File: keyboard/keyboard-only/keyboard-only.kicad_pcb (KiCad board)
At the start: 2 copper layers, 3.6 x 3.1 mm, 203 parts, among them J1 USB_C_Receptacle_USB2.0, SW1 SW_PUSH, SW10 SW_PUSH, SW11 SW_PUSH, SW12 SW_PUSH, SW13 SW_PUSH, SW14 SW_PUSH, SW15 SW_PUSH, SW16 SW_PUSH, SW17 SW_PUSH, SW18 SW_PUSH, SW19 SW_PUSH, SW2 SW_PUSH, SW20 SW_PUSH, SW21 SW_PUSH, SW22 SW_PUSH, SW23 SW_PUSH, SW24 SW_PUSH, SW25 SW_PUSH, SW26 SW_PUSH, SW27 SW_PUSH, SW28 SW_PUSH, SW29 SW_PUSH, SW3 SW_PUSH, SW30 SW_PUSH, SW31 SW_PUSH, SW32 SW_PUSH, SW33 SW_PUSH, SW34 SW_PUSH, SW35 SW_PUSH, SW36 SW_PUSH, SW37 SW_PUSH, SW38 SW_PUSH, SW39 SW_PUSH, SW4 SW_PUSH, SW40 SW_PUSH, SW41 SW_PUSH, SW42 SW_PUSH, SW43 SW_PUSH, SW44 SW_PUSH, SW45 SW_PUSH, SW46 SW_PUSH, SW47 SW_PUSH, SW48 SW_PUSH, SW49 SW_PUSH, SW5 SW_PUSH, SW50 SW_PUSH, SW51 SW_PUSH, SW52 SW_PUSH, SW53 SW_PUSH, SW54 SW_PUSH, SW55 SW_PUSH, SW56 SW_PUSH, SW57 SW_PUSH, SW58 SW_PUSH, SW59 SW_PUSH, SW6 SW_PUSH, SW60 SW_PUSH, SW7 SW_PUSH, SW8 SW_PUSH, SW9 SW_PUSH, U1 ATmega16U4-AU, Y1 16MHz

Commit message: Add net name for rows and columns
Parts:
- moved LED53 260.5 mm to (29.4, 144.7)
- moved D62 249.8 mm to (19.3, 158.1)
- moved LED49 242.1 mm to (20.5, 149.5)
- moved LED4 236.5 mm to (56.2, 149.5)
- moved SW8 233.9 mm to (26.1, 112.0)
- moved LED47 225.6 mm to (38.3, 144.7)
- moved D34 224.7 mm to (45.5, 158.1)
- moved D35 216.4 mm to (236.8, 75.6)
- moved LED57 200.8 mm to (91.8, 149.5)
- moved D59 189.7 mm to (71.7, 158.1)
- moved LED30 189.6 mm to (222.5, 73.5)
- moved SW38 188.8 mm to (86.7, 91.8)
- moved D10 179.4 mm to (221.3, 87.4)
- moved D48 177.2 mm to (78.2, 158.1)
- moved SW28 175.6 mm to (207.9, 31.2)
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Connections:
- D10 pad 1: N$35 -> ROW0
- D10 pad 2: N$17 -> N$27
- D11 pad 1: N$38 (its old number) -> ROW0
- D11 pad 2: N$17 -> N$29
- D12 pad 1: N$41 -> ROW0
- D12 pad 2: N$17 -> N$31
- D13 pad 1: N$44 (its old number) -> ROW0
- D13 pad 2: N$17 -> N$33
- D14 pad 1: N$47 -> ROW0
- D14 pad 2: N$17 -> N$35
- D15 pad 1: N$50 (its old number) -> ROW0
- D15 pad 2: N$17 -> N$37
- D16 pad 1: N$52 (its old number) -> ROW1
- D16 pad 2: N$53 -> N$39
- D17 pad 1: N$55 -> ROW1
- D17 pad 2: N$53 -> N$41
- D18 pad 1: N$57 -> ROW1
- D18 pad 2: N$53 -> N$43
- D19 pad 1: N$59 -> ROW1
- D19 pad 2: N$53 -> N$45
- D20 pad 1: N$61 -> ROW1
- D20 pad 2: N$53 -> N$47
- D21 pad 1: N$63 -> ROW1
- D21 pad 2: N$53 -> N$49
- D22 pad 1: N$65 -> ROW1
- D22 pad 2: N$53 -> N$51
- D23 pad 1: N$67 -> ROW1
- D24 pad 1: N$69 -> ROW1
- D24 pad 2: N$53 -> N$55
- D25 pad 1: N$71 -> ROW1
- D25 pad 2: N$53 -> N$57
- D26 pad 1: N$73 -> ROW1
- D26 pad 2: N$53 -> N$59
- D27 pad 1: N$75 -> ROW1
- D27 pad 2: N$53 -> N$61
- D28 pad 1: N$77 -> ROW2
- D28 pad 2: N$78 (its old number) -> N$63
- D29 pad 1: N$80 (its old number) -> ROW2
- D29 pad 2: N$78 (its old number) -> N$65
- D30 pad 1: N$82 (its old number) -> ROW2
- D30 pad 2: N$78 (its old number) -> N$67
- D31 pad 1: N$84 (its old number) -> ROW2
- D31 pad 2: N$78 (its old number) -> N$69
- D32 pad 1: N$86 (its old number) -> ROW2
- D32 pad 2: N$78 (its old number) -> N$71
- D33 pad 1: N$88 (its old number) -> ROW2
- D33 pad 2: N$78 (its old number) -> N$73
- D34 pad 1: N$90 (its old number) -> ROW2
- D34 pad 2: N$78 (its old number) -> N$75
- D35 pad 1: N$92 (its old number) -> ROW2
- D35 pad 2: N$78 (its old number) -> N$77
- D36 pad 1: N$94 (its old number) -> ROW2
- D36 pad 2: N$78 (its old number) -> N$79
- D37 pad 1: N$96 (its old number) -> ROW2
- D37 pad 2: N$78 (its old number) -> N$81
- D38 pad 1: N$98 (its old number) -> ROW2
- D38 pad 2: N$78 (its old number) -> N$83
- D39 pad 1: N$100 (its old number) -> ROW2
- D39 pad 2: N$78 (its old number) -> N$85
- D4 pad 1: N$16 (its old number) -> ROW0
- D4 pad 2: N$17 -> N$15
- D40 pad 1: N$102 (its old number) -> ROW3
- D40 pad 2: N$103 -> N$87
- D41 pad 1: N$105 -> ROW3
- D41 pad 2: N$103 -> N$89
- D42 pad 1: N$107 -> ROW3
- D42 pad 2: N$103 -> N$91
- D43 pad 1: N$109 -> ROW3
- D43 pad 2: N$103 -> N$93
- D44 pad 1: N$111 -> ROW3
- D44 pad 2: N$103 -> N$95
- D45 pad 1: N$113 -> ROW3
- D45 pad 2: N$103 -> N$97
- D46 pad 1: N$115 -> ROW3
- D46 pad 2: N$103 -> N$99
- D47 pad 1: N$117 -> ROW3
- D47 pad 2: N$103 -> N$101
- D48 pad 1: N$119 -> ROW3
- D49 pad 1: N$121 -> ROW3
- D49 pad 2: N$103 -> N$105
- D5 pad 1: N$20 (its old number) -> ROW0
- D50 pad 1: N$123 -> ROW3
- D50 pad 2: N$103 -> N$107
- D51 pad 1: N$125 -> ROW3
- D51 pad 2: N$103 -> N$109
- D52 pad 1: N$127 -> ROW4
- D52 pad 2: N$128 (its old number) -> N$111
- D53 pad 1: N$130 (its old number) -> ROW4
- D53 pad 2: N$128 (its old number) -> N$113
- D54 pad 1: N$132 (its old number) -> ROW4
- D54 pad 2: N$128 (its old number) -> N$115
- D55 pad 1: N$134 (its old number) -> ROW4
- D55 pad 2: N$128 (its old number) -> N$117
- D56 pad 1: N$136 -> ROW4
- D56 pad 2: N$128 (its old number) -> N$119
- D57 pad 1: N$138 -> ROW4
- D57 pad 2: N$128 (its old number) -> N$121
- D58 pad 1: N$140 -> ROW4
- D58 pad 2: N$128 (its old number) -> N$123
- D59 pad 1: N$142 -> ROW4
- D59 pad 2: N$128 (its old number) -> N$125
- D6 pad 1: N$23 -> ROW0
- D6 pad 2: N$17 -> N$19
- D60 pad 1: N$144 -> ROW4
- D60 pad 2: N$128 (its old number) -> N$127
- D61 pad 1: N$146 -> ROW4
- D61 pad 2: N$128 (its old number) -> N$129
- D62 pad 1: N$148 -> ROW4
- D62 pad 2: N$128 (its old number) -> N$131
- D63 pad 1: N$150 -> ROW4
- D63 pad 2: N$128 (its old number) -> N$133
- D7 pad 1: N$26 (its old number) -> ROW0
- D7 pad 2: N$17 -> N$21
- D8 pad 1: N$29 -> ROW0
- D8 pad 2: N$17 -> N$23
- D9 pad 1: N$32 (its old number) -> ROW0
- D9 pad 2: N$17 -> N$25
- SW1 pad 1: N$15 -> COL0
- SW1 pad 2: N$16 (its old number) -> N$15
- SW10 pad 1: N$43 -> COL9
- SW10 pad 2: N$44 (its old number) -> N$33
- SW11 pad 1: N$46 (its old number) -> COL10
- SW11 pad 2: N$47 -> N$35
- SW12 pad 1: N$49 -> COL11
- SW12 pad 2: N$50 (its old number) -> N$37
- SW13 pad 1: N$15 -> COL0
- SW13 pad 2: N$52 (its old number) -> N$39
- SW14 pad 1: N$19 -> COL1
- SW14 pad 2: N$55 -> N$41
- SW15 pad 1: N$22 (its old number) -> COL2
- SW15 pad 2: N$57 -> N$43
- SW16 pad 1: N$25 -> COL3
- SW16 pad 2: N$59 -> N$45
- SW17 pad 1: N$28 (its old number) -> COL4
- SW17 pad 2: N$61 -> N$47
- SW18 pad 1: N$31 -> COL5
- SW18 pad 2: N$63 -> N$49
- SW19 pad 1: N$34 (its old number) -> COL6
- SW19 pad 2: N$65 -> N$51
- SW2 pad 1: N$19 -> COL1
- SW2 pad 2: N$20 (its old number) -> N$17
- SW20 pad 1: N$37 -> COL7
- SW20 pad 2: N$67 -> N$53
- SW21 pad 1: N$40 (its old number) -> COL8
- SW21 pad 2: N$69 -> N$55
- SW22 pad 1: N$43 -> COL9
- SW22 pad 2: N$71 -> N$57
- SW23 pad 1: N$46 (its old number) -> COL10
- SW23 pad 2: N$73 -> N$59
- SW24 pad 1: N$49 -> COL11
- SW24 pad 2: N$75 -> N$61
- SW25 pad 1: N$15 -> COL0
- SW25 pad 2: N$77 -> N$63
- SW26 pad 1: N$19 -> COL1
- SW26 pad 2: N$80 (its old number) -> N$65
- SW27 pad 1: N$22 (its old number) -> COL2
- SW27 pad 2: N$82 (its old number) -> N$67
- SW28 pad 1: N$25 -> COL3
- SW28 pad 2: N$84 (its old number) -> N$69
- SW29 pad 1: N$28 (its old number) -> COL4
- SW29 pad 2: N$86 (its old number) -> N$71
- SW3 pad 1: N$22 (its old number) -> COL2
- SW3 pad 2: N$23 -> N$19
- SW30 pad 1: N$31 -> COL5
- SW30 pad 2: N$88 (its old number) -> N$73
- SW31 pad 1: N$34 (its old number) -> COL6
- SW31 pad 2: N$90 (its old number) -> N$75
- SW32 pad 1: N$37 -> COL7
- SW32 pad 2: N$92 (its old number) -> N$77
- SW33 pad 1: N$40 (its old number) -> COL8
- SW33 pad 2: N$94 (its old number) -> N$79
- SW34 pad 1: N$43 -> COL9
- SW34 pad 2: N$96 (its old number) -> N$81
- SW35 pad 1: N$46 (its old number) -> COL10
- SW35 pad 2: N$98 (its old number) -> N$83
- SW36 pad 1: N$49 -> COL11
- SW36 pad 2: N$100 (its old number) -> N$85
- SW37 pad 1: N$15 -> COL0
- SW37 pad 2: N$102 (its old number) -> N$87
- SW38 pad 1: N$19 -> COL1
- SW38 pad 2: N$105 -> N$89
- SW39 pad 1: N$22 (its old number) -> COL2
- SW39 pad 2: N$107 -> N$91
- SW4 pad 1: N$25 -> COL3
- SW4 pad 2: N$26 (its old number) -> N$21
- SW40 pad 1: N$25 -> COL3
- SW40 pad 2: N$109 -> N$93
- SW41 pad 1: N$28 (its old number) -> COL4
- SW41 pad 2: N$111 -> N$95
- SW42 pad 1: N$31 -> COL5
- SW42 pad 2: N$113 -> N$97
- SW43 pad 1: N$34 (its old number) -> COL6
- SW43 pad 2: N$115 -> N$99
- SW44 pad 1: N$37 -> COL7
- SW44 pad 2: N$117 -> N$101
- SW45 pad 1: N$40 (its old number) -> COL8
- SW45 pad 2: N$119 -> N$103
- SW46 pad 1: N$43 -> COL9
- SW46 pad 2: N$121 -> N$105
- SW47 pad 1: N$46 (its old number) -> COL10
- SW47 pad 2: N$123 -> N$107
- SW48 pad 1: N$49 -> COL11
- SW48 pad 2: N$125 -> N$109
- SW49 pad 1: N$15 -> COL0
- SW49 pad 2: N$127 -> N$111
- SW5 pad 1: N$28 (its old number) -> COL4
- SW5 pad 2: N$29 -> N$23
- SW50 pad 1: N$19 -> COL1
- SW50 pad 2: N$130 (its old number) -> N$113
- SW51 pad 1: N$22 (its old number) -> COL2
- SW51 pad 2: N$132 (its old number) -> N$115
- SW52 pad 1: N$25 -> COL3
- SW52 pad 2: N$134 (its old number) -> N$117
- SW53 pad 1: N$28 (its old number) -> COL4
- SW53 pad 2: N$136 -> N$119
- SW54 pad 1: N$31 -> COL5
- SW54 pad 2: N$138 -> N$121
- SW55 pad 1: N$34 (its old number) -> COL6
- SW55 pad 2: N$140 -> N$123
- SW56 pad 1: N$37 -> COL7
- SW56 pad 2: N$142 -> N$125
- SW57 pad 1: N$40 (its old number) -> COL8
- SW57 pad 2: N$144 -> N$127
- SW58 pad 1: N$43 -> COL9
- SW58 pad 2: N$146 -> N$129
- SW59 pad 1: N$46 (its old number) -> COL10
- SW59 pad 2: N$148 -> N$131
- SW6 pad 1: N$31 -> COL5
- SW6 pad 2: N$32 (its old number) -> N$25
- SW60 pad 1: N$49 -> COL11
- SW60 pad 2: N$150 -> N$133
- SW7 pad 1: N$34 (its old number) -> COL6
- SW7 pad 2: N$35 -> N$27
- SW8 pad 1: N$37 -> COL7
- SW8 pad 2: N$38 (its old number) -> N$29
- SW9 pad 1: N$40 (its old number) -> COL8
- SW9 pad 2: N$41 -> N$31
- U1 pad 1: N$103 -> ROW3
- U1 pad 10: N$37 -> COL7
- U1 pad 11: N$40 (its old number) -> COL8
- U1 pad 12: N$49 -> COL11
- U1 pad 25: N$17 -> ROW0
- U1 pad 27: N$78 (its old number) -> ROW2
- U1 pad 28: N$128 (its old number) -> ROW4
- U1 pad 29: N$43 -> COL9
- U1 pad 30: N$46 (its old number) -> COL10
- U1 pad 31: N$53 -> ROW1
- U1 pad 36: N$31 -> COL5
- U1 pad 37: N$28 (its old number) -> COL4
- U1 pad 38: N$25 -> COL3
- U1 pad 39: N$22 (its old number) -> COL2
- U1 pad 40: N$19 -> COL1
- U1 pad 41: N$15 -> COL0
- U1 pad 9: N$34 (its old number) -> COL6

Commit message: Flip everything to bottom of pcb
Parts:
- C1, C2, C3, C4, C5, C6, C7, C8, D1, D10, D11, D12, D13, D14, D15, D16, D17, D18, D19, D2, D20, D21, D22, D23, D24, D25, D26, D27, D28, D29, D3, D30, D31, D32, D33, D34, D35, D36, D37, D38, D39, D4, D40, D41, D42, D43, D44, D45, D46, D47, D48, D49, D5, D50, D51, D52, D53, D54, D55, D56, D57, D58, D59, D6, D60, D61, D62, D63, D7, D8, D9, F1, J1, LED1, LED10, LED11, LED12, LED13, LED14, LED15, LED16, LED17, LED18, LED19, LED2, LED20, LED21, LED22, LED23, LED24, LED25, LED26, LED27, LED28, LED29, LED3, LED30, LED31, LED32, LED33, LED34, LED35, LED36, LED37, LED38, LED39, LED4, LED40, LED41, LED42, LED43, LED44, LED45, LED46, LED47, LED48, LED49, LED5, LED50, LED51, LED52, LED53, LED54, LED55, LED56, LED57, LED58, LED59, LED6, LED60, LED7, LED8, LED9, R1, R2, R3, R4, R5, R6, R7, R8, U1, Y1: moved to B.Cu

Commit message: Organize key matrix and diodes
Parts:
- moved D62 240.1 mm to (254.0, 107.3), turned to 90 degrees
- moved R2 238.6 mm to (40.6, 40.0)
- moved R1 238.5 mm to (40.7, 35.3)
- moved J1 232.6 mm to (38.1, 26.0)
- moved SW12 223.1 mm to (265.4, 31.1)
- moved SW36 222.4 mm to (265.4, 69.2)
- moved SW11 220.3 mm to (246.4, 31.1)
- moved SW35 209.7 mm to (246.4, 69.2)
- moved D50 207.5 mm to (254.0, 88.3), turned to 90 degrees
- moved D52 194.1 mm to (63.5, 107.3), turned to 90 degrees
- moved LED10 188.2 mm to (202.1, 225.3)
- moved LED30 188.2 mm to (172.9, 255.2)
- moved LED31 188.2 mm to (193.1, 239.8)
- moved LED35 188.2 mm to (193.1, 225.3)
- moved LED44 188.2 mm to (181.9, 250.3)
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
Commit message: Setup LEDs
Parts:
- moved LED49 334.0 mm to (227.3, 55.2)
- moved LED53 329.7 mm to (246.4, 74.3)
- moved LED48 326.1 mm to (227.3, 74.3)
- moved LED60 312.8 mm to (265.4, 36.2)
- moved LED54 304.7 mm to (246.4, 93.3)
- moved LED47 295.9 mm to (227.3, 93.3)
- moved LED59 293.5 mm to (265.4, 55.3)
- moved LED52 289.5 mm to (246.4, 55.2)
- moved LED38 289.1 mm to (189.2, 74.3)
- moved LED46 289.1 mm to (227.3, 112.4)
- moved LED57 285.2 mm to (265.4, 93.3)
- moved LED58 284.5 mm to (265.4, 74.3)
- moved LED56 277.9 mm to (265.4, 112.4)
- moved LED39 267.6 mm to (189.2, 55.2)
- moved LED50 266.7 mm to (227.3, 36.2)
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
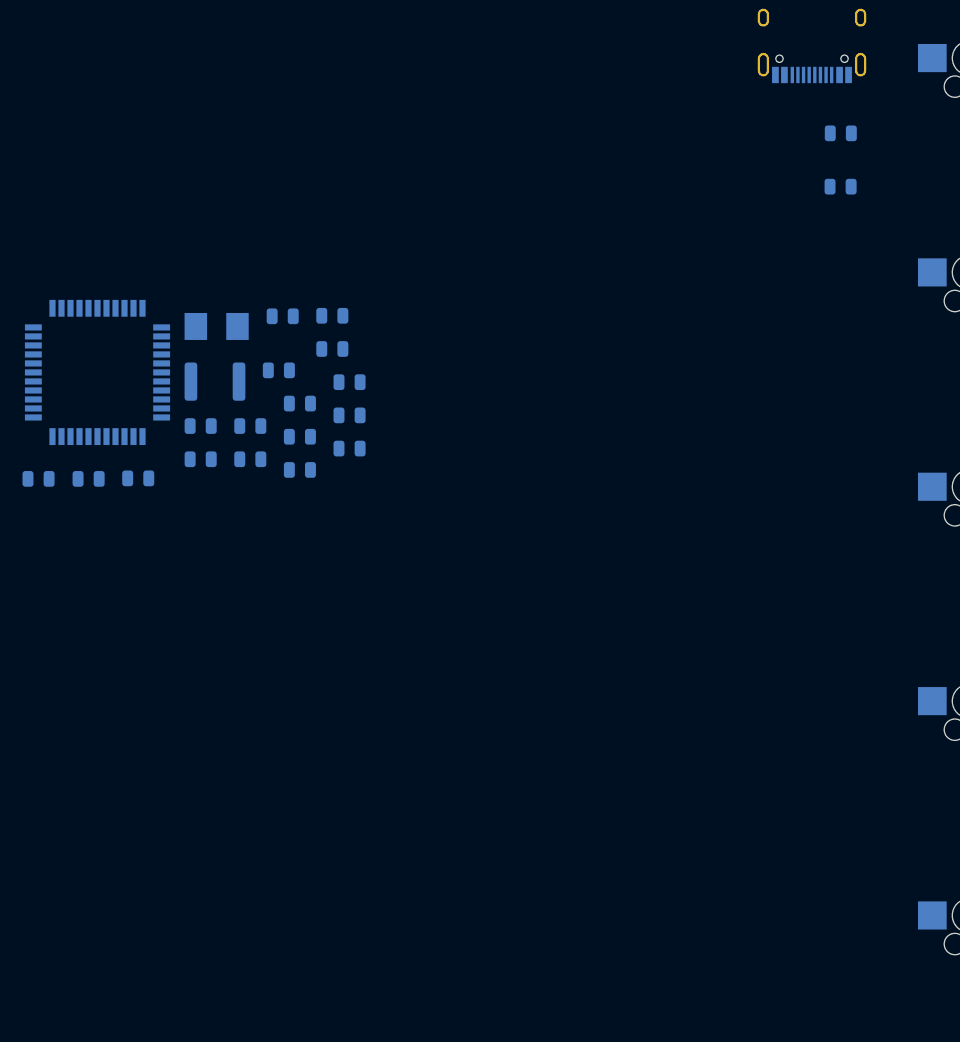
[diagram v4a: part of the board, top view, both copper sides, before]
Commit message: Base ProMicro layout
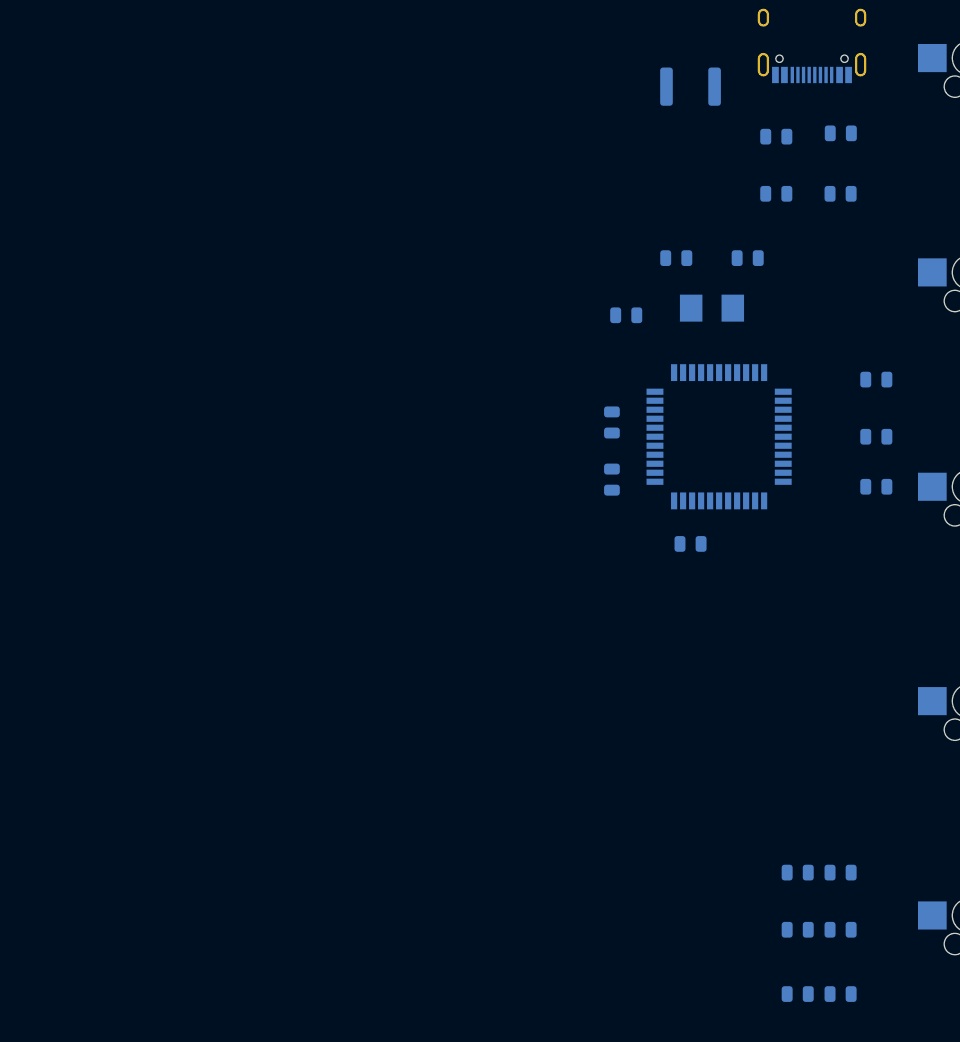
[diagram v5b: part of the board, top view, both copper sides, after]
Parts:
- moved D1 81.0 mm to (40.6, 111.8)
- moved D3 79.4 mm to (40.6, 101.0)
- moved D2 73.7 mm to (40.6, 106.0)
- moved R5 68.3 mm to (36.8, 101.0)
- moved R4 67.6 mm to (36.8, 106.0)
- moved R3 62.7 mm to (36.8, 111.8)
- moved C2 55.7 mm to (43.8, 62.2)
- moved U1 55.5 mm to (29.8, 62.2)
- moved R8 53.4 mm to (34.9, 35.6)
- moved C4 51.4 mm to (43.8, 66.7)
- moved F1 49.7 mm to (27.3, 31.1), turned to 180 degrees
- moved C3 48.7 mm to (43.8, 57.1)
- moved Y1 44.1 mm to (29.2, 50.8), turned to 180 degrees
- moved C7 42.8 mm to (32.4, 46.4)
- moved R7 42.7 mm to (34.9, 40.6)
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
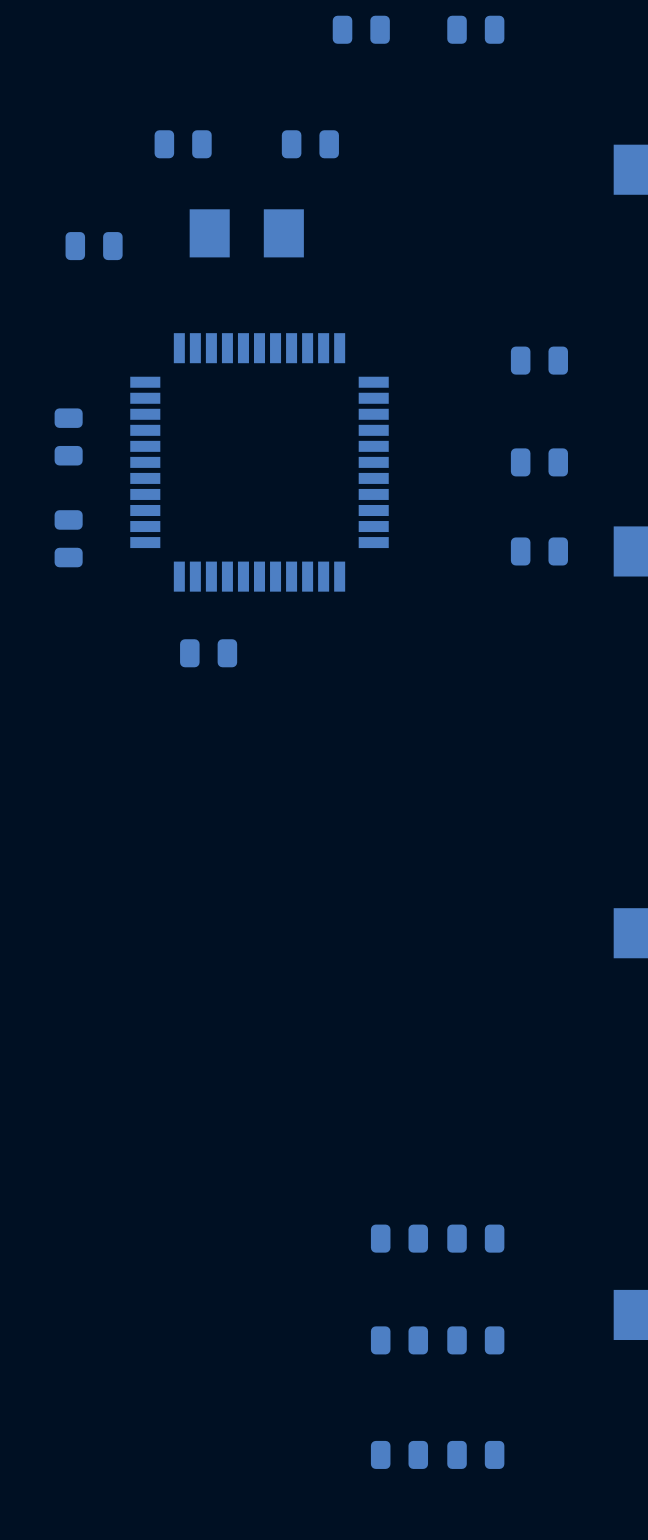
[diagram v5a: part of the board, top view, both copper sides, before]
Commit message: Reorient LEDs
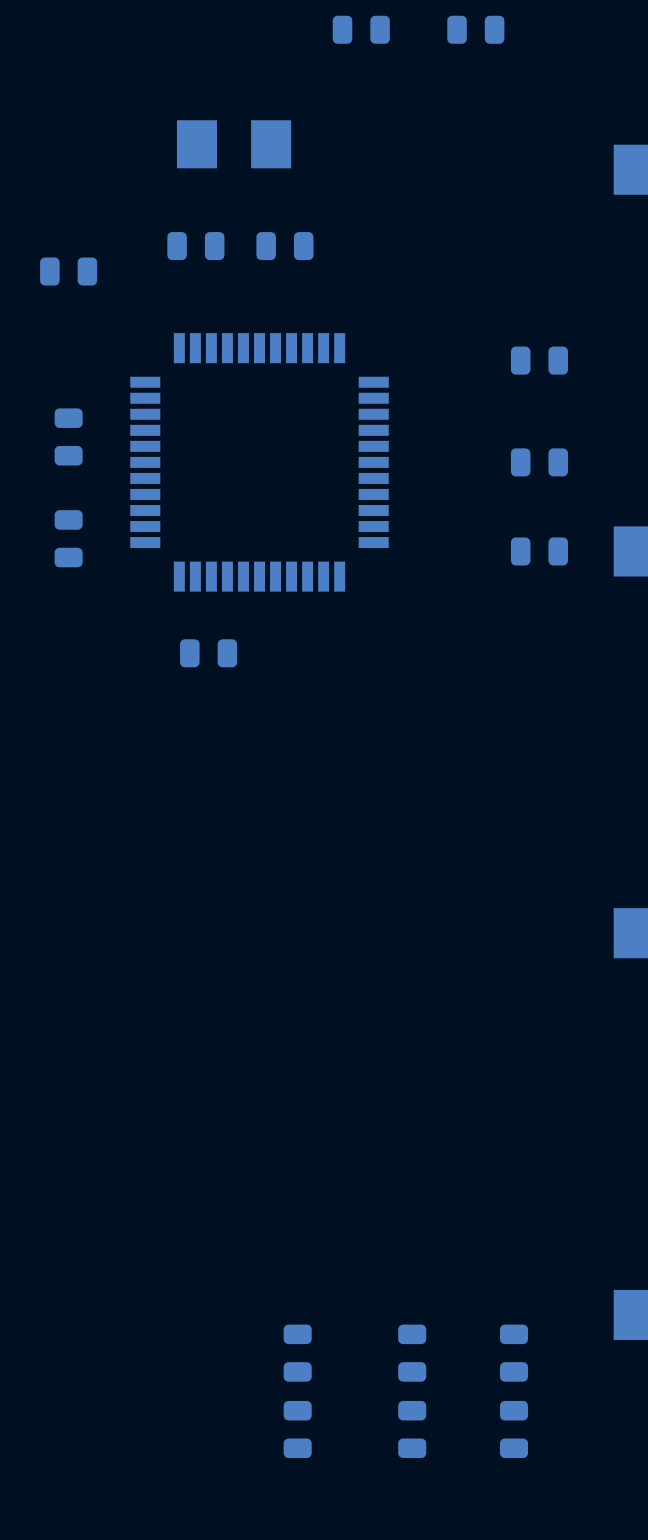
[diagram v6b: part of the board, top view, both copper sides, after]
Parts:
- moved D3 9.71 mm to (42.5, 110.5), turned to 270 degrees
- moved D1 8.98 mm to (31.8, 110.5), turned to 270 degrees
- moved R5 8.08 mm to (42.5, 106.7), turned to 270 degrees
- moved R3 7.18 mm to (31.8, 106.7), turned to 270 degrees
- moved D2 5.46 mm to (37.5, 110.5), turned to 270 degrees
- moved C7 5.24 mm to (31.1, 51.4)
- moved C8 5.12 mm to (26.7, 51.4)
- moved Y1 4.49 mm to (28.6, 46.4)
- moved R6 1.80 mm to (20.3, 52.7)
- moved R4 0.90 mm to (37.5, 106.7), turned to 270 degrees

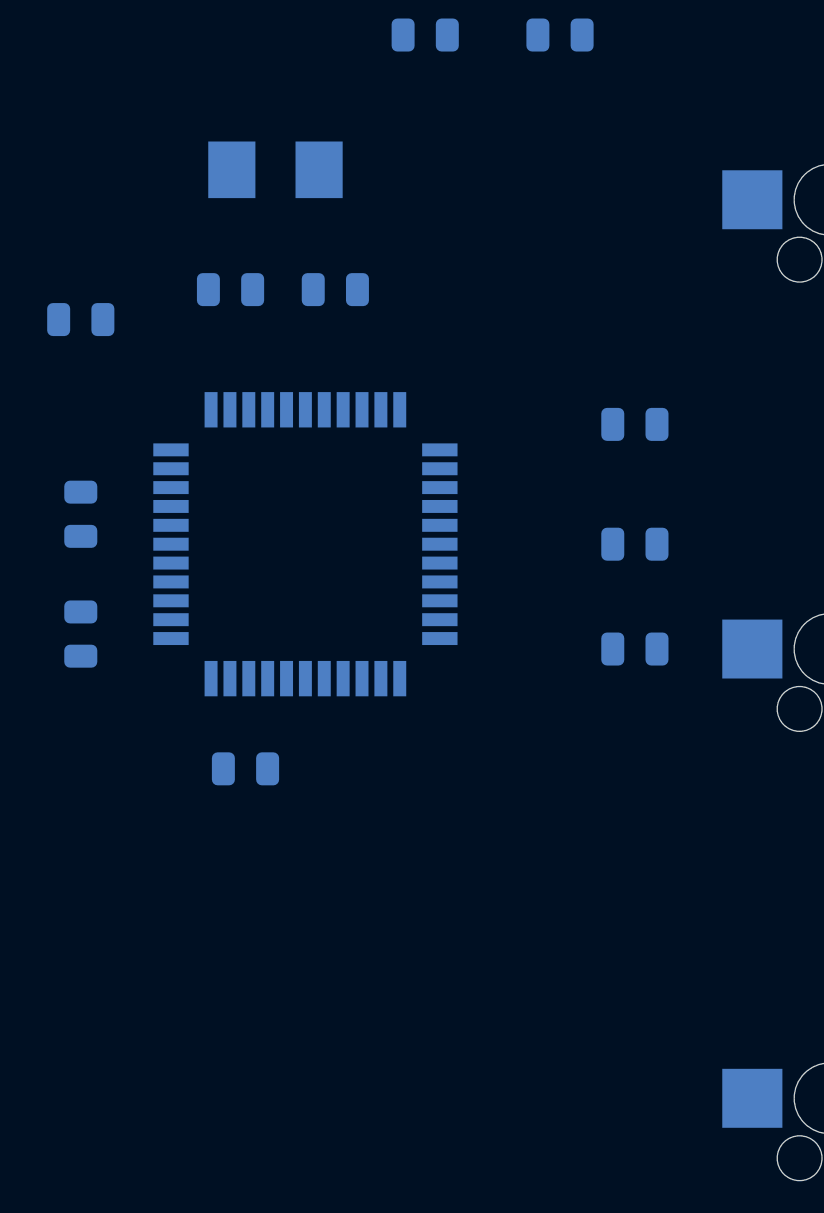
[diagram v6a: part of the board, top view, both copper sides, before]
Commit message: Layout ProMicro better
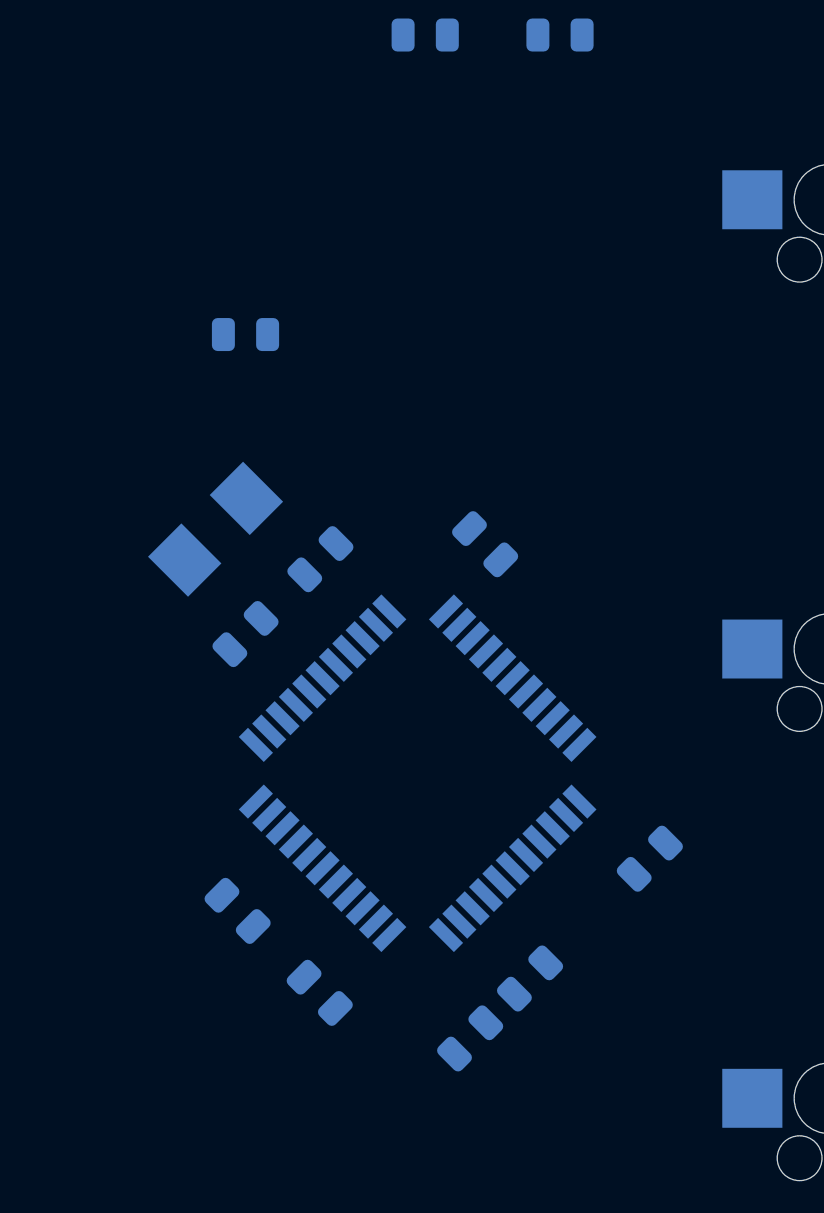
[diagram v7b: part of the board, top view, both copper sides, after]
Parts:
- moved C2 22.1 mm to (36.8, 83.2), turned to 45 degrees
- moved C3 18.4 mm to (44.5, 75.6), turned to 225 degrees
- moved C5 18.3 mm to (30.5, 81.3), turned to 315 degrees
- moved C1 18.1 mm to (27.0, 77.8), turned to 315 degrees
- moved Y1 15.5 mm to (26.0, 61.6), turned to 225 degrees
- moved C6 15.0 mm to (39.4, 80.6), turned to 225 degrees
- moved C8 14.6 mm to (27.3, 66.0), turned to 225 degrees
- moved C7 11.4 mm to (30.5, 62.9), turned to 45 degrees
- moved U1 10.8 mm to (34.6, 71.9), turned to 45 degrees
- moved C4 7.75 mm to (37.5, 62.2), turned to 135 degrees
- moved R6 7.01 mm to (27.3, 53.3)

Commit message: Add board outline
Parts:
- moved J1 0.64 mm to (38.1, 25.4)
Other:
- board size 3.6 x 3.1 mm -> 252.7 x 94 mm
- net class Power/GND added: clearance 0.2, trace_width 0.5, via_dia 0.8, via_drill 0.4
